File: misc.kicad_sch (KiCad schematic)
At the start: 23 parts, among them J7 Conn_ARM_JTAG_SWD_10, SW2 SW_DIP_x02, U1 MIMX8MM6DVTLZAA, Y3 24Mhz

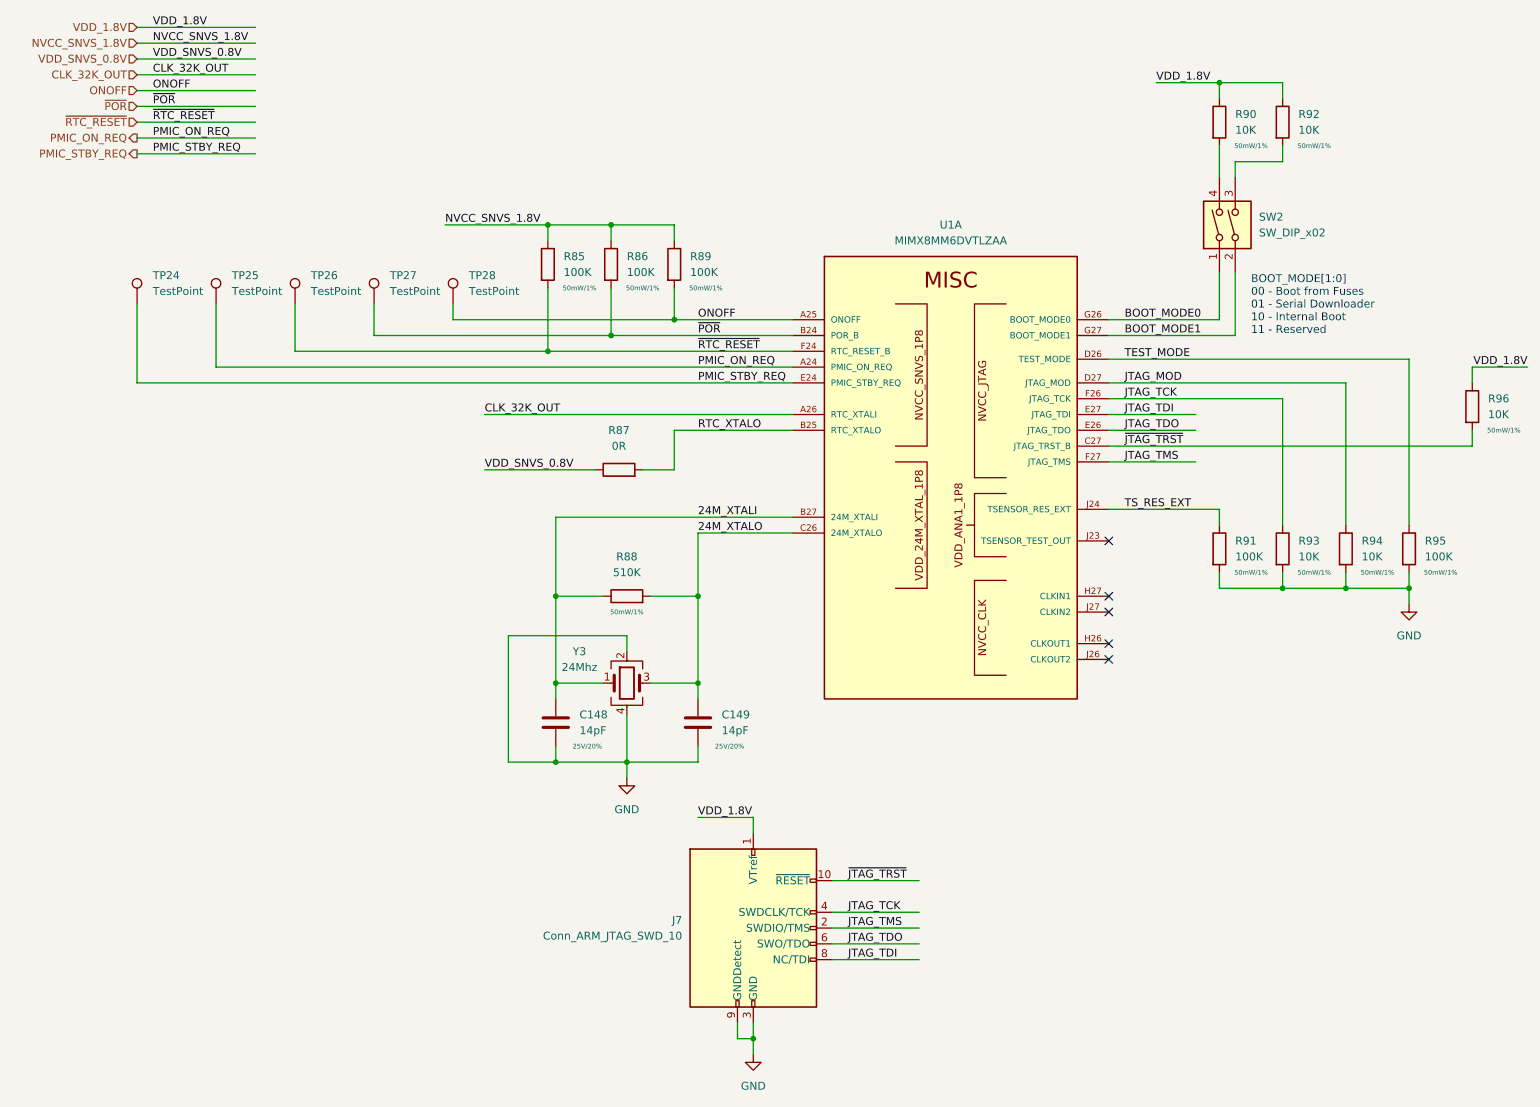
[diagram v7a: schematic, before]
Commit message: inital routing of ddr data bus, sch work
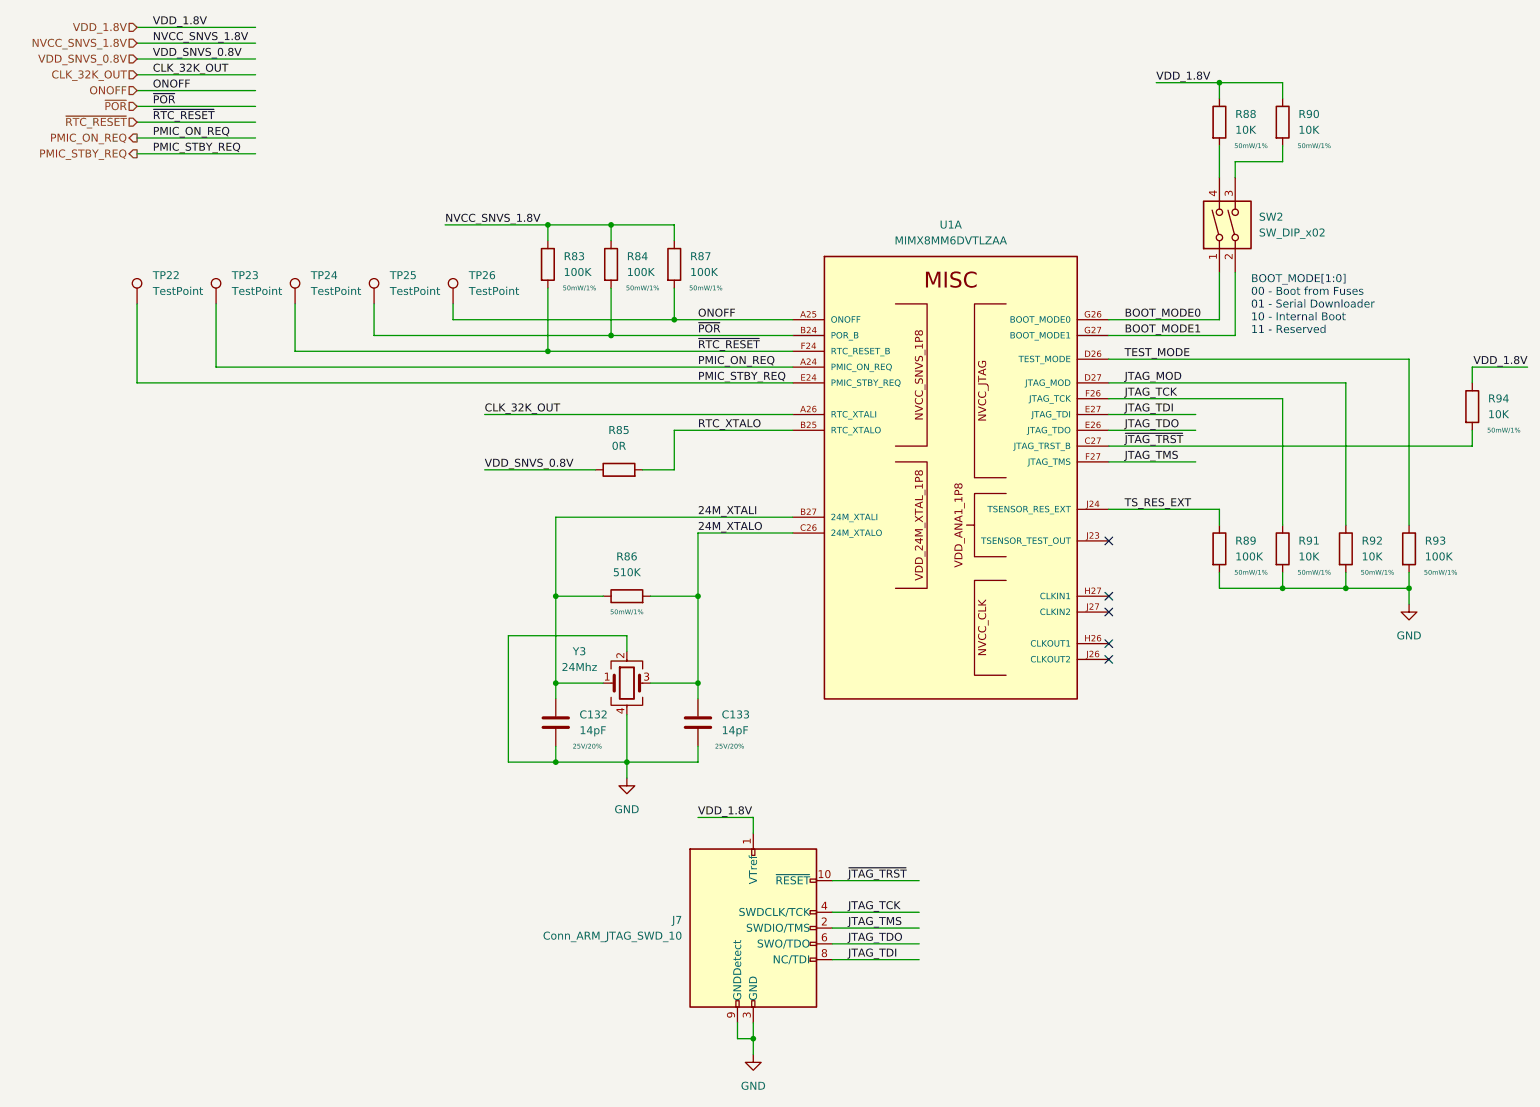
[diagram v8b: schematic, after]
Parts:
- renumbered C148 to C132, C149 to C133, R85 to R83, R86 to R84, R87 to R85, R88 to R86, R89 to R87, R90 to R88, R91 to R89, R92 to R90, R93 to R91, R94 to R92, R95 to R93, R96 to R94, TP24 to TP22, TP25 to TP23, TP26 to TP24, TP27 to TP25, TP28 to TP26
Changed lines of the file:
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@@
   (symbol (lib_id "Device:C") (at 97.79 132.08 0) (unit 1)
     (in_bom yes) (on_board yes)
-    (property "Reference" "C148" (id 0) (at 101.6 130.8099 0)
+    (property "Reference" "C132" (id 0) (at 101.6 130.8099 0)
       (effects (font (size 1.27 1.27)) (justify left))
     )
@@
   (symbol (lib_id "Device:R") (at 224.79 104.14 0) (unit 1)
     (in_bom yes) (on_board yes)
-    (property "Reference" "R94" (id 0) (at 227.33 102.8699 0)
+    (property "Reference" "R92" (id 0) (at 227.33 102.8699 0)
       (effects (font (size 1.27 1.27)) (justify left))
     )
@@
   (symbol (lib_id "Connector:TestPoint") (at 81.28 64.77 0) (unit 1)
     (in_bom yes) (on_board yes) (fields_autoplaced)
-    (property "Reference" "TP28" (id 0) (at 83.82 60.1979 0)
+    (property "Reference" "TP26" (id 0) (at 83.82 60.1979 0)
       (effects (font (size 1.27 1.27)) (justify left))
     )
@@
   (symbol (lib_id "power:GND") (at 129.54 185.42 0) (unit 1)
     (in_bom yes) (on_board yes) (fields_autoplaced)
-    (property "Reference" "#PWR0137" (id 0) (at 129.54 191.77 0)
+    (property "Reference" "#PWR0128" (id 0) (at 129.54 191.77 0)
       (effects (font (size 1.27 1.27)) hide)
     )
@@
   (symbol (lib_id "Device:R") (at 214.63 35.56 0) (unit 1)
     (in_bom yes) (on_board yes)
-    (property "Reference" "R92" (id 0) (at 217.17 34.2899 0)
+    (property "Reference" "R90" (id 0) (at 217.17 34.2899 0)
       (effects (font (size 1.27 1.27)) (justify left))
     )
@@
   (symbol (lib_id "Connector:TestPoint") (at 68.58 64.77 0) (unit 1)
     (in_bom yes) (on_board yes) (fields_autoplaced)
-    (property "Reference" "TP27" (id 0) (at 71.12 60.1979 0)
+    (property "Reference" "TP25" (id 0) (at 71.12 60.1979 0)
       (effects (font (size 1.27 1.27)) (justify left))
     )
@@
   (symbol (lib_id "Device:R") (at 204.47 35.56 0) (unit 1)
     (in_bom yes) (on_board yes)
-    (property "Reference" "R90" (id 0) (at 207.01 34.2899 0)
+    (property "Reference" "R88" (id 0) (at 207.01 34.2899 0)
       (effects (font (size 1.27 1.27)) (justify left))
     )
@@
   (symbol (lib_id "Device:R") (at 96.52 58.42 0) (unit 1)
     (in_bom yes) (on_board yes)
-    (property "Reference" "R85" (id 0) (at 99.06 57.1499 0)
+    (property "Reference" "R83" (id 0) (at 99.06 57.1499 0)
       (effects (font (size 1.27 1.27)) (justify left))
     )
@@
   (symbol (lib_id "Device:R") (at 109.22 111.76 90) (unit 1)
     (in_bom yes) (on_board yes)
-    (property "Reference" "R88" (id 0) (at 109.22 105.41 90))
+    (property "Reference" "R86" (id 0) (at 109.22 105.41 90))
     (property "Value" "510K" (id 1) (at 109.22 107.95 90))
     (property "Footprint" "Resistor_SMD:R_0402_1005Metric" (id 2) (at 109.22 113.538 90)
@@
   (symbol (lib_id "power:GND") (at 109.22 140.97 0) (unit 1)
     (in_bom yes) (on_board yes) (fields_autoplaced)
-    (property "Reference" "#PWR0136" (id 0) (at 109.22 147.32 0)
+    (property "Reference" "#PWR0127" (id 0) (at 109.22 147.32 0)
       (effects (font (size 1.27 1.27)) hide)
     )
@@
   (symbol (lib_id "Connector:TestPoint") (at 55.88 64.77 0) (unit 1)
     (in_bom yes) (on_board yes) (fields_autoplaced)
-    (property "Reference" "TP26" (id 0) (at 58.42 60.1979 0)
+    (property "Reference" "TP24" (id 0) (at 58.42 60.1979 0)
       (effects (font (size 1.27 1.27)) (justify left))
     )
@@
   (symbol (lib_id "Device:R") (at 234.95 104.14 0) (unit 1)
     (in_bom yes) (on_board yes)
-    (property "Reference" "R95" (id 0) (at 237.49 102.8699 0)
+    (property "Reference" "R93" (id 0) (at 237.49 102.8699 0)
       (effects (font (size 1.27 1.27)) (justify left))
     )
@@
   (symbol (lib_id "Device:R") (at 214.63 104.14 0) (unit 1)
     (in_bom yes) (on_board yes)
-    (property "Reference" "R93" (id 0) (at 217.17 102.8699 0)
+    (property "Reference" "R91" (id 0) (at 217.17 102.8699 0)
       (effects (font (size 1.27 1.27)) (justify left))
     )
@@
   (symbol (lib_id "Device:R") (at 116.84 58.42 0) (unit 1)
     (in_bom yes) (on_board yes)
-    (property "Reference" "R89" (id 0) (at 119.38 57.1499 0)
+    (property "Reference" "R87" (id 0) (at 119.38 57.1499 0)
       (effects (font (size 1.27 1.27)) (justify left))
     )
@@
   (symbol (lib_id "power:GND") (at 234.95 113.03 0) (unit 1)
     (in_bom yes) (on_board yes) (fields_autoplaced)
-    (property "Reference" "#PWR0138" (id 0) (at 234.95 119.38 0)
+    (property "Reference" "#PWR0129" (id 0) (at 234.95 119.38 0)
       (effects (font (size 1.27 1.27)) hide)
     )
@@
   (symbol (lib_id "Device:R") (at 204.47 104.14 0) (unit 1)
     (in_bom yes) (on_board yes)
-    (property "Reference" "R91" (id 0) (at 207.01 102.8699 0)
+    (property "Reference" "R89" (id 0) (at 207.01 102.8699 0)
       (effects (font (size 1.27 1.27)) (justify left))
     )
@@
   (symbol (lib_id "Device:C") (at 120.65 132.08 0) (unit 1)
     (in_bom yes) (on_board yes)
-    (property "Reference" "C149" (id 0) (at 124.46 130.8099 0)
+    (property "Reference" "C133" (id 0) (at 124.46 130.8099 0)
       (effects (font (size 1.27 1.27)) (justify left))
     )
@@
   (symbol (lib_id "Device:R") (at 245.11 81.28 0) (unit 1)
     (in_bom yes) (on_board yes)
-    (property "Reference" "R96" (id 0) (at 247.65 80.0099 0)
+    (property "Reference" "R94" (id 0) (at 247.65 80.0099 0)
       (effects (font (size 1.27 1.27)) (justify left))
     )
@@
   (symbol (lib_id "Connector:TestPoint") (at 30.48 64.77 0) (unit 1)
     (in_bom yes) (on_board yes) (fields_autoplaced)
-    (property "Reference" "TP24" (id 0) (at 33.02 60.1979 0)
+    (property "Reference" "TP22" (id 0) (at 33.02 60.1979 0)
       (effects (font (size 1.27 1.27)) (justify left))
     )
@@
   (symbol (lib_id "Device:R") (at 106.68 58.42 0) (unit 1)
     (in_bom yes) (on_board yes)
-    (property "Reference" "R86" (id 0) (at 109.22 57.1499 0)
+    (property "Reference" "R84" (id 0) (at 109.22 57.1499 0)
       (effects (font (size 1.27 1.27)) (justify left))
     )
@@
   (symbol (lib_id "Device:R") (at 107.95 91.44 90) (unit 1)
     (in_bom yes) (on_board yes) (fields_autoplaced)
-    (property "Reference" "R87" (id 0) (at 107.95 85.09 90))
+    (property "Reference" "R85" (id 0) (at 107.95 85.09 90))
     (property "Value" "0R" (id 1) (at 107.95 87.63 90))
     (property "Footprint" "Resistor_SMD:R_0402_1005Metric" (id 2) (at 107.95 93.218 90)
@@
   (symbol (lib_id "Connector:TestPoint") (at 43.18 64.77 0) (unit 1)
     (in_bom yes) (on_board yes) (fields_autoplaced)
-    (property "Reference" "TP25" (id 0) (at 45.72 60.1979 0)
-      (effects (font (size 1.27 1.27)) (justify left))
-    )
+    (property "Reference" "TP23" (id 0) (at 45.72 60.1979 0)
+      (effects (font (size 1.27 1.27)) (justify left))
+    )
